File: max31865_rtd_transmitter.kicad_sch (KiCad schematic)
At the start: 0 parts

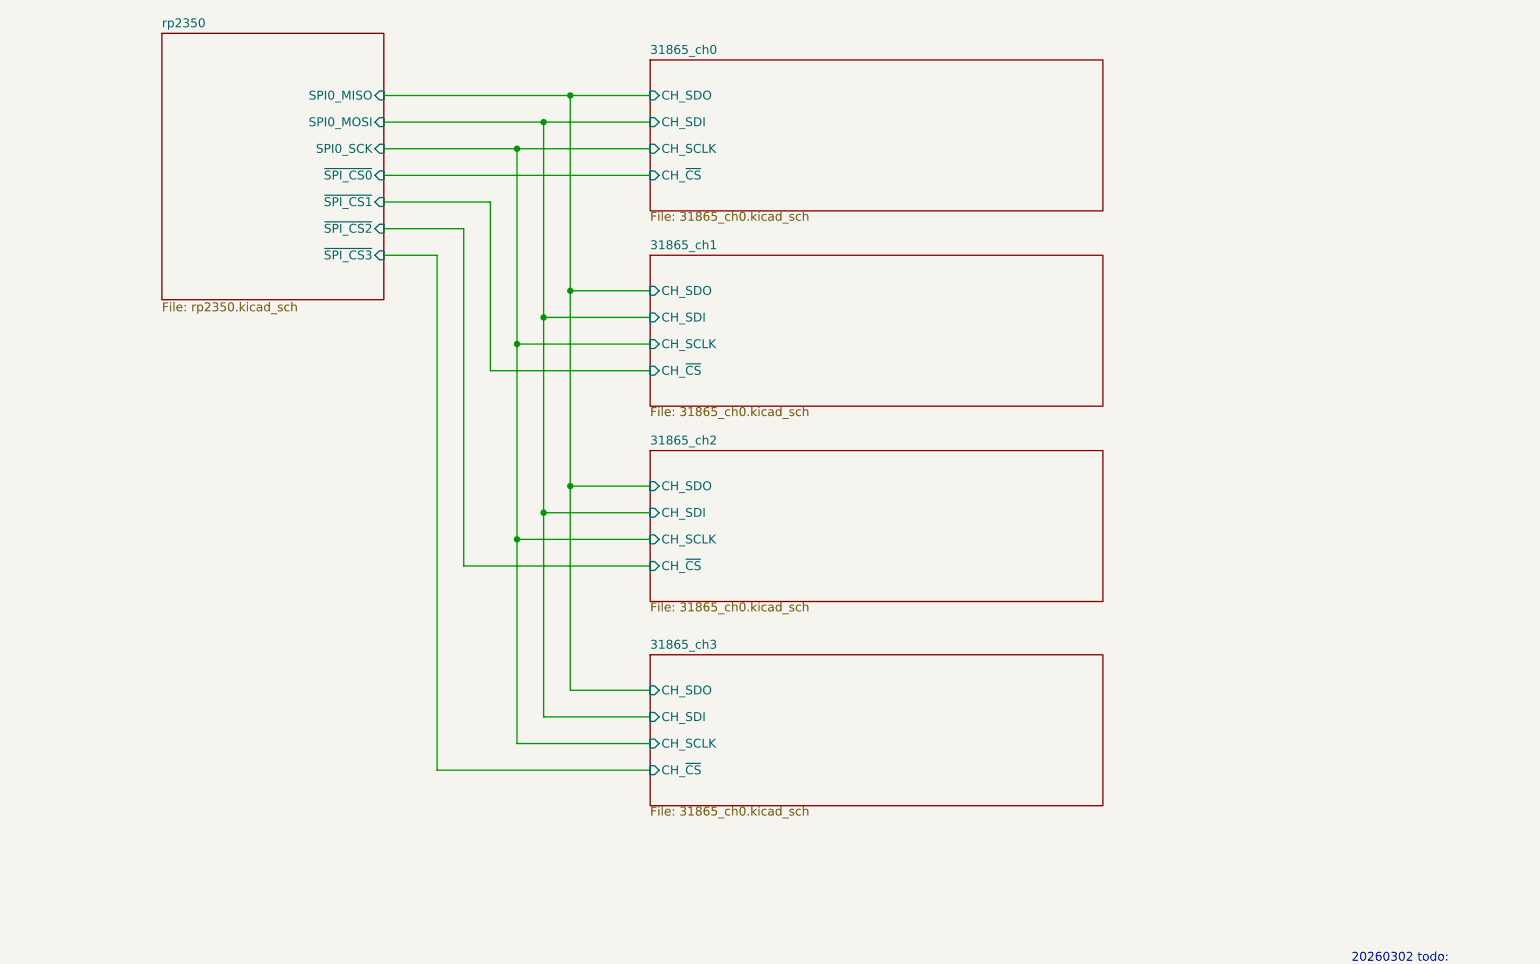
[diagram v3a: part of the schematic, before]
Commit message: start pcb layout, add sd card and screen
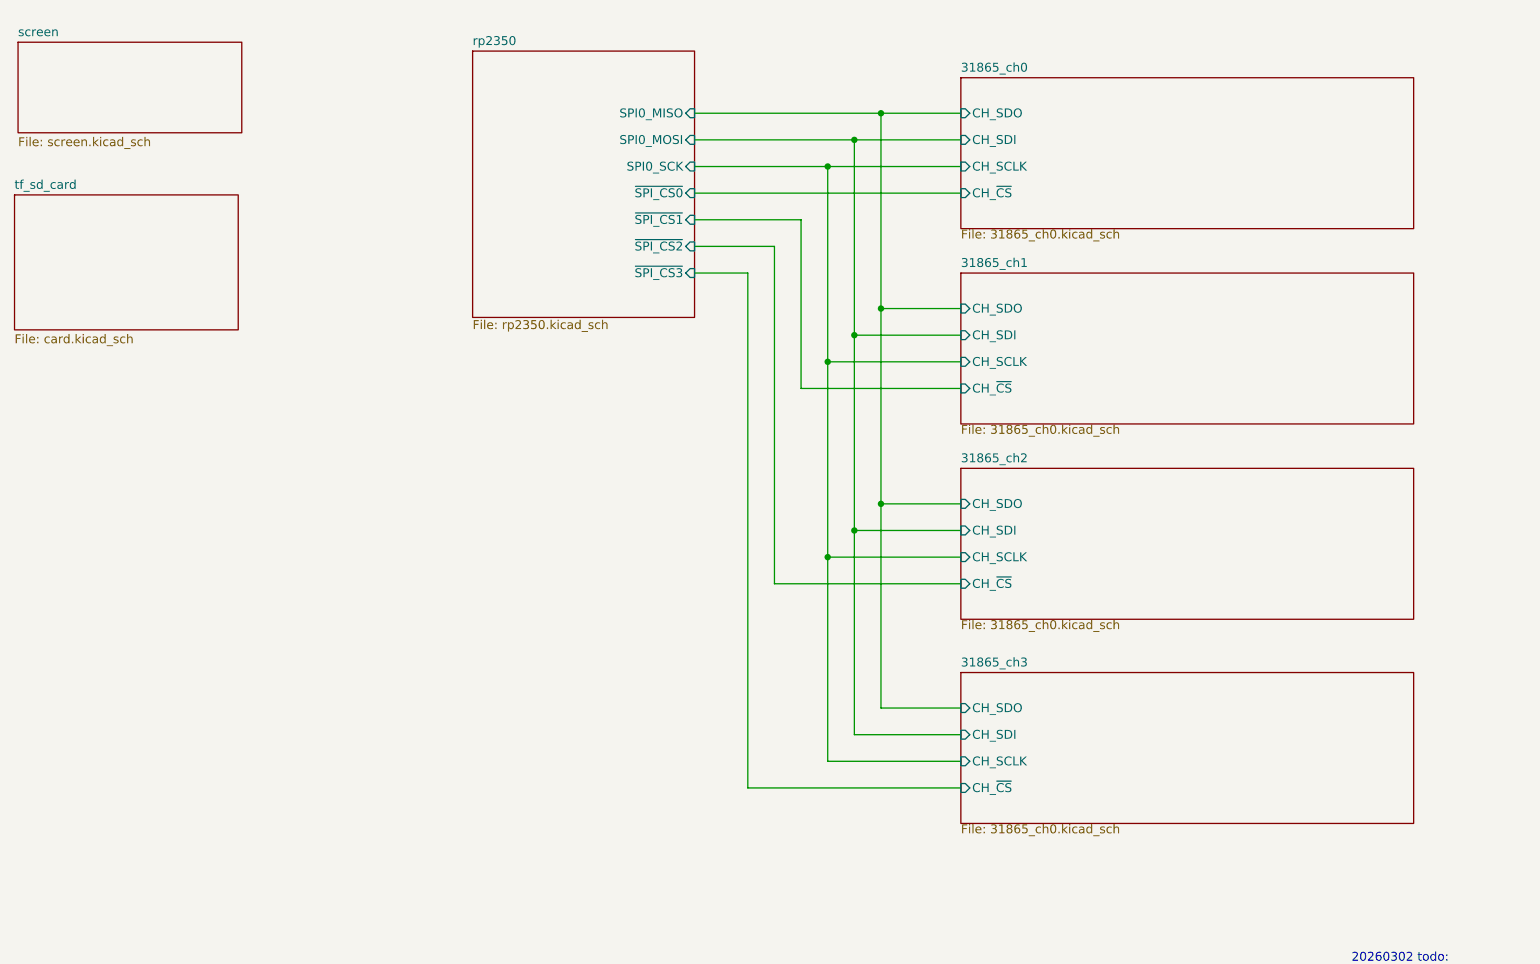
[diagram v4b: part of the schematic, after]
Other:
- added sheet screen (screen.kicad_sch)
- added sheet tf_sd_card (card.kicad_sch)
